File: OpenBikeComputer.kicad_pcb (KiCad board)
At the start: 4 copper layers, 80 x 80 mm, 56 parts, among them J1 USB_C_Receptacle_USB2.0_14P, J2 RJ45_Shielded, J3 RJ45_Shielded, J4 Micro_SD_Card_Det1, J5 Conn_01x24_Socket, J6 Conn_01x03_Pin, J7 Conn_01x05_Pin, U1 nRF52840-QIXX, U2 nPM1300-QEXX, U3 BQ298012RUGR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

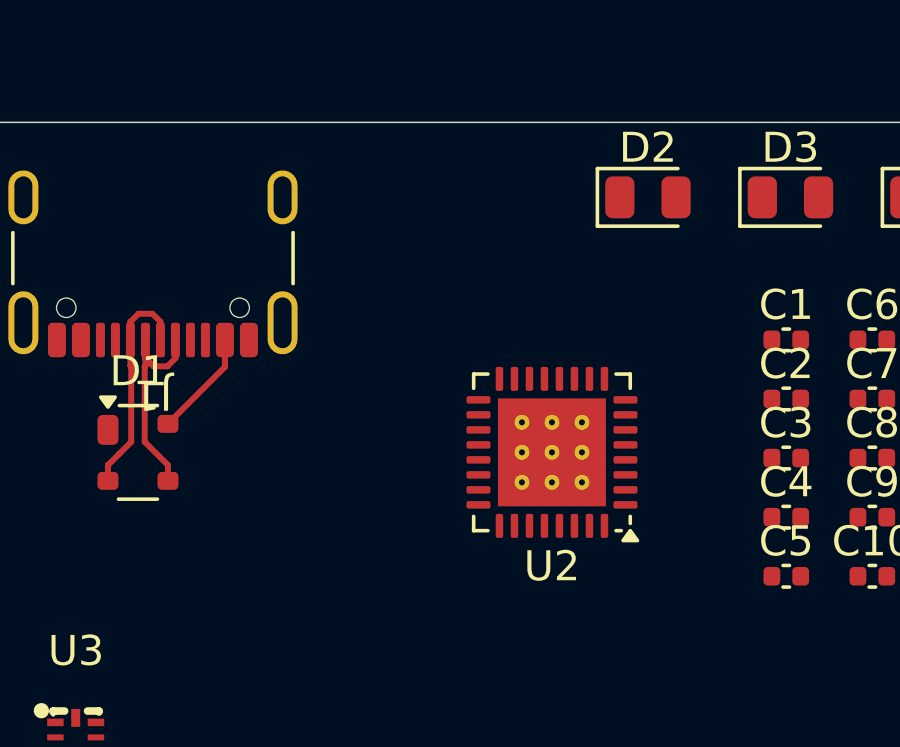
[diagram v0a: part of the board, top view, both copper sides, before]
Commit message: add inductor and crystal
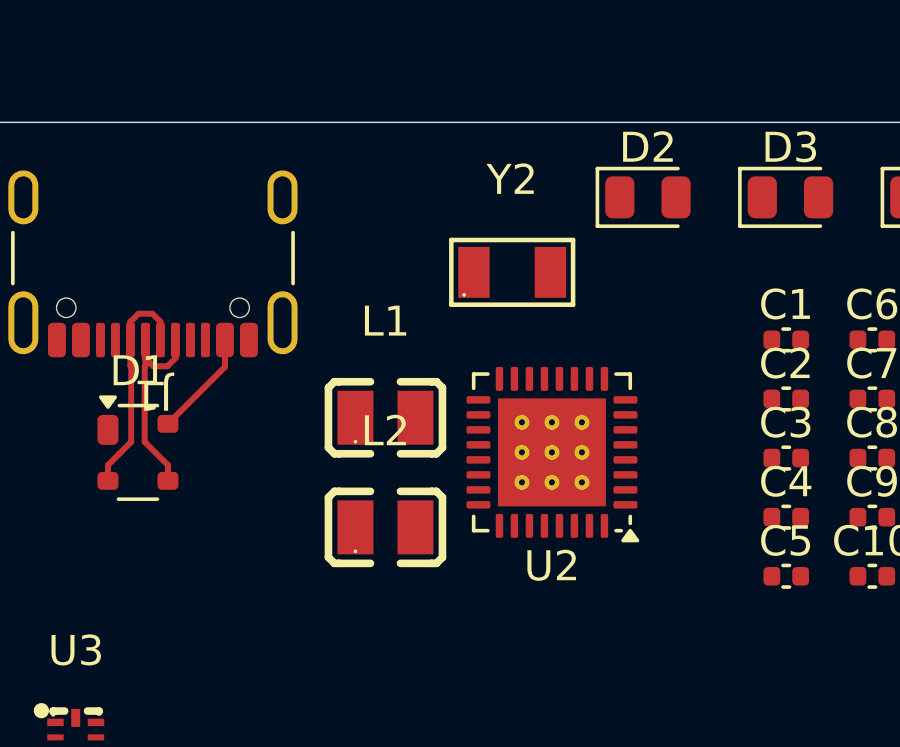
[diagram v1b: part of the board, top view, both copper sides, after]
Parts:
- added L1: 2.2uH, Library:L0806, F.Cu at (199.5, 84.8)
- added L2: 2.2uH, Library:L0806, F.Cu at (199.5, 88.5)
- added Y2: 32.768KHz, Library:CRYSTAL-SMD_L3.2-W1.5-1, F.Cu at (203.7, 80.0)

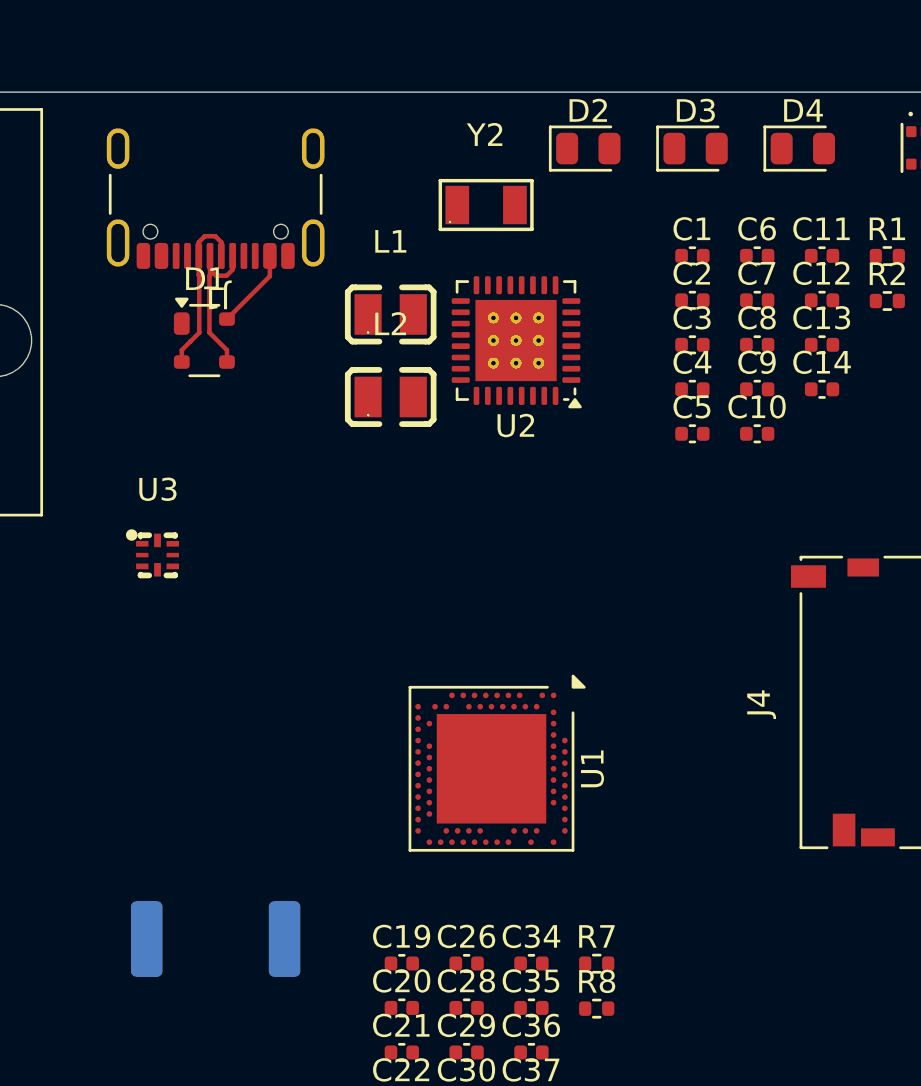
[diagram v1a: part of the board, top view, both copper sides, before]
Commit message: fixup design pcb clearances
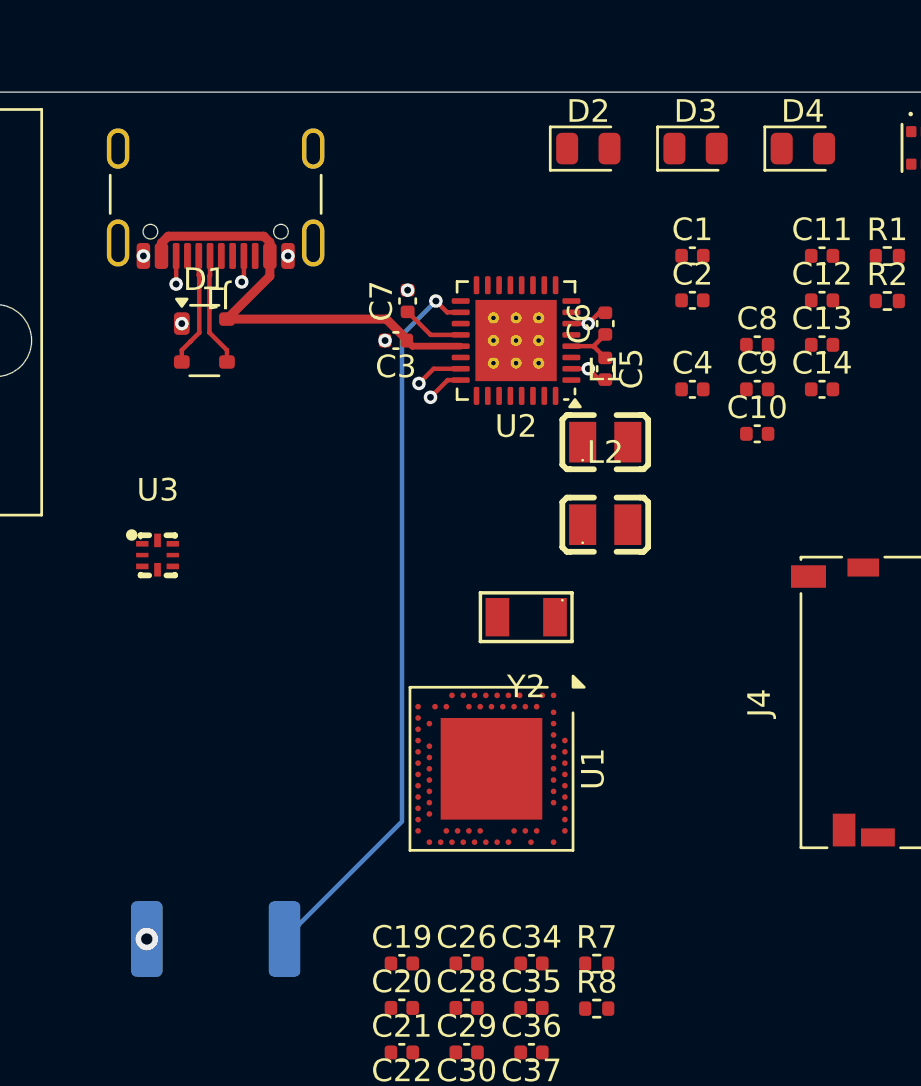
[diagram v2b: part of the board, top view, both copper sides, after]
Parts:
- moved Y2 18.3 mm to (205.5, 98.2), turned to 180 degrees
- moved C7 15.5 mm to (200.2, 84.2), turned to 90 degrees
- moved C3 13.1 mm to (199.7, 86.0), turned to 180 degrees
- moved L1 11.1 mm to (209.0, 90.5)
- moved L2 11.1 mm to (209.0, 94.2)
- moved C6 7.37 mm to (209.0, 85.2), turned to 90 degrees
- moved C5 4.82 mm to (209.0, 87.2), turned to -90 degrees
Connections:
- C5 pad 2: PVSS1 -> GND
- C6 pad 2: PVSS2 -> GND
- C8 pad 2: PVSS1 -> GND
- C9 pad 2: PVSS2 -> GND
- U2 pad 2: PVSS1 -> GND
- U2 pad 6: PVSS2 -> GND
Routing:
- net /Battery/NTC: track 0.00 -> 32.3 mm, vias 0 -> 1
- net VBUSIN: track 3.58 -> 20.7 mm
- net CC2: track 0.00 -> 16.4 mm, vias 0 -> 2
- net CC1: track 0.00 -> 13.1 mm, vias 0 -> 2
- net VSYS: track 0.00 -> 5.22 mm
- net GND: track 0.00 -> 3.40 mm, vias 0 -> 8
- net D-: track 7.46 -> 5.03 mm
- net D+: track 7.46 -> 5.03 mm

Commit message: use separate i2c bus for PMIC
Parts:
- added R10: 10k, Resistor_SMD:R_0402_1005Metric, F.Cu at (208.6, 120.0)
- added R9: 10k, Resistor_SMD:R_0402_1005Metric, F.Cu at (208.6, 118.0)
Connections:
- R7 pad 2: /MCU/SCL -> /MCU/SCL1
- R8 pad 2: /MCU/SDA -> /MCU/SDA1
- U1 pad AC15: unconnected-(U1-P0.19-PadAC15) -> /MCU/SDA2
- U1 pad AD20: unconnected-(U1-P0.24-PadAD20) -> /MCU/SCL2
- U1 pad L1: /MCU/SDA -> /MCU/SDA1
- U1 pad N1: /MCU/SCL -> /MCU/SCL1
- U2 pad 13: /MCU/SDA -> /MCU/SDA1
- U2 pad 14: /MCU/SCL -> /MCU/SCL1
- U2 pad 15: unconnected-(U2-SHPHLD-Pad15) -> Net-(U2-SHPHLD)
- U6 pad 13: /MCU/SCL -> /MCU/SCL2
- U6 pad 14: /MCU/SDA -> /MCU/SDA2
- U7 pad 3: /MCU/SDA -> /MCU/SDA2
- U7 pad 4: /MCU/SCL -> /MCU/SCL2
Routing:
- net D-: track 5.03 -> 7.46 mm
- net D+: track 5.03 -> 7.46 mm

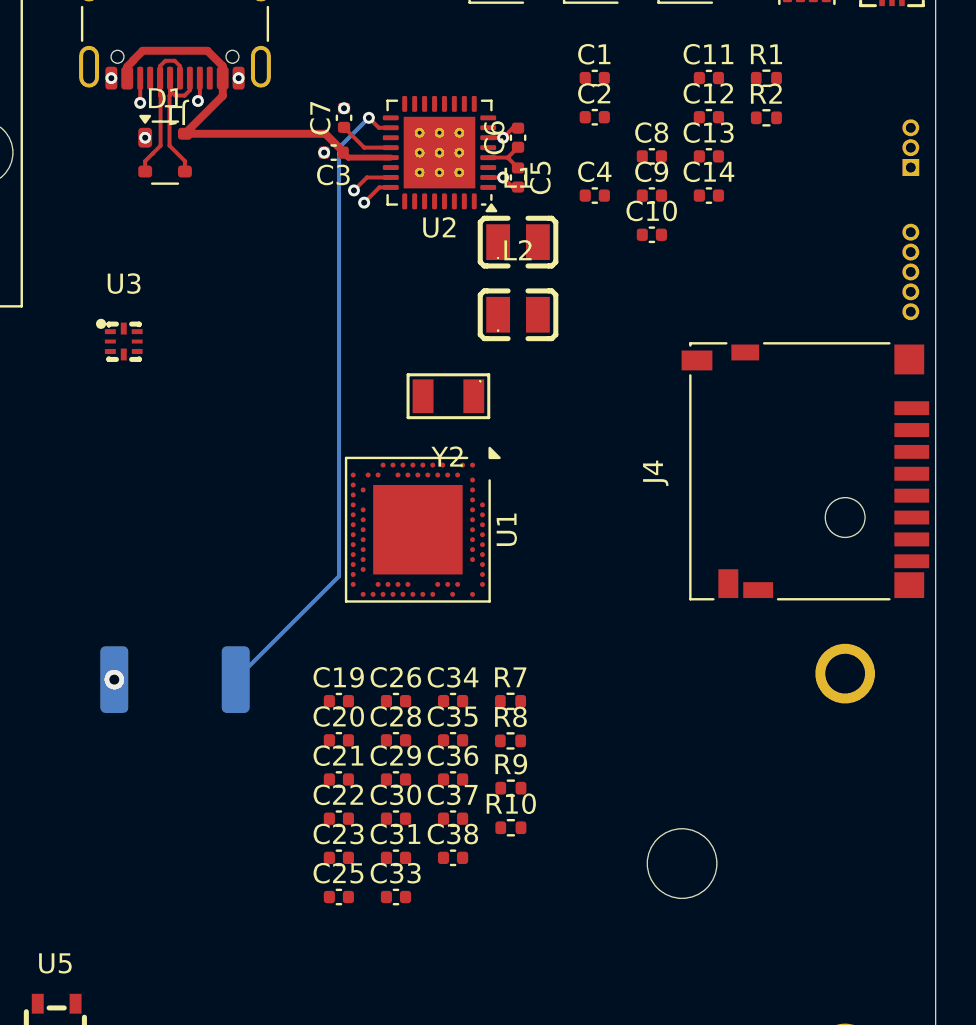
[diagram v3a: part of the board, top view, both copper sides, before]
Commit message: switch out SoC, stuff is in the air
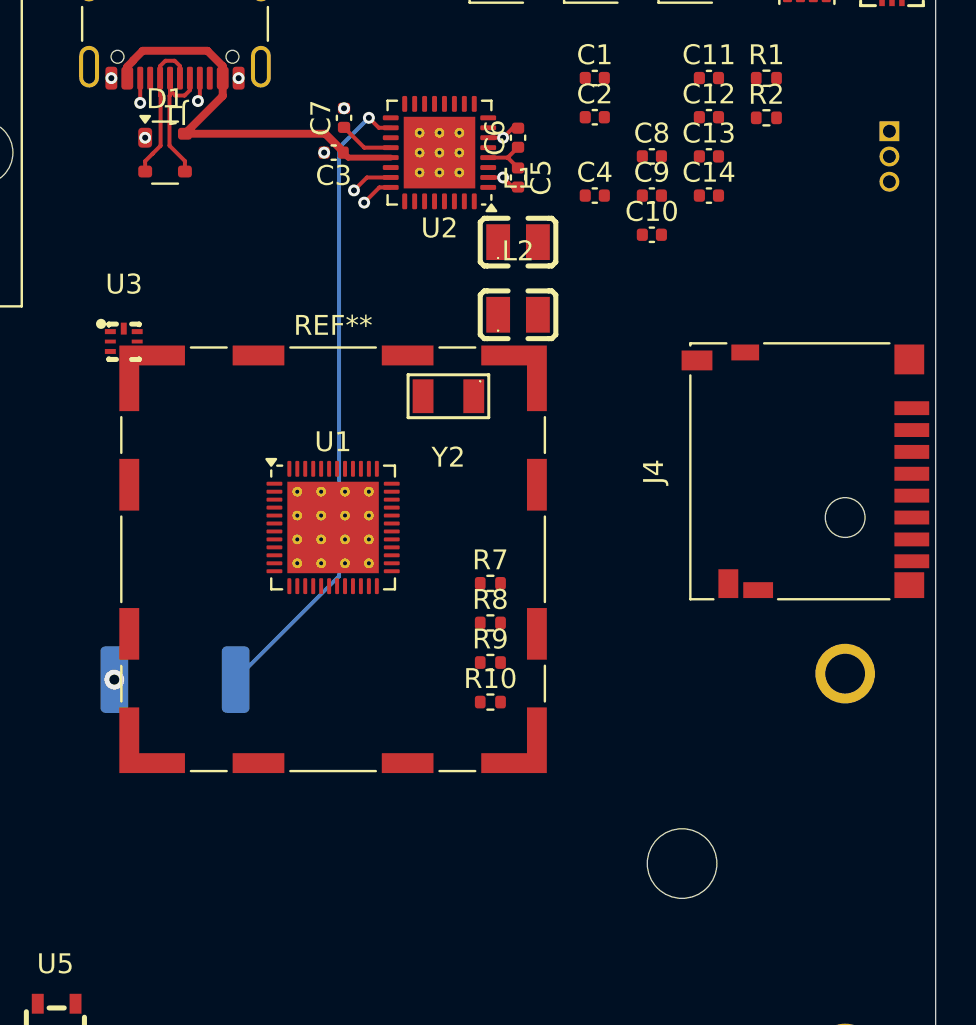
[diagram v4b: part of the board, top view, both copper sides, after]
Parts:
- removed C19, C20, C21, C22: 12pF, Capacitor_SMD:C_0402_1005Metric
- removed C23, C34: 4.7uF, Capacitor_SMD:C_0402_1005Metric
- removed C25, C35, C36, C38: 100nF, Capacitor_SMD:C_0402_1005Metric
- removed C26: 100pF, Capacitor_SMD:C_0402_1005Metric
- removed C28: 820pF, Capacitor_SMD:C_0402_1005Metric
- removed C29, C37: 1.0uF, Capacitor_SMD:C_0402_1005Metric
- removed C30: 47nF, Capacitor_SMD:C_0402_1005Metric
- removed C31, C33: 0.5pF, Capacitor_SMD:C_0402_1005Metric
- removed J7: Conn_01x05_Pin, Connector_PinHeader_1.00mm:PinHeader_1x05_P1.00mm_Vertical
- added REF**: Wuerth_36103205_20x20mm, RF_Shielding:Wuerth_36103205_20x20mm, F.Cu at (199.7, 106.5)
- J6: footprint Connector_PinHeader_1.00mm:PinHeader_1x03_P1.00mm_Vertical -> Connector_PinHeader_1.27mm:PinHeader_1x03_P1.27mm_Vertical
- U1: value nRF52840-QIXX -> nRF54L15-QFXX; footprint Package_DFN_QFN:Nordic_AQFN-73-1EP_7x7mm_P0.5mm -> Package_DFN_QFN:QFN-48-1EP_6x6mm_P0.4mm_EP4.6x4.6mm_ThermalVias
- moved R10 6.40 mm to (207.6, 113.6)
- moved R9 6.40 mm to (207.6, 111.6)
- moved R7 6.02 mm to (207.6, 107.7)
- moved R8 6.02 mm to (207.6, 109.7)
- moved U1 4.26 mm to (199.7, 104.8), turned to 0 degrees
- moved J6 1.09 mm to (227.7, 84.9)
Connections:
- C4 pad 1: /MCU/VBUS -> /Power/VUSBOUT
- D1 pad 2: D+ -> unconnected-(D1-I/O1-Pad2)
- D1 pad 3: D- -> unconnected-(D1-I/O2-Pad3)
- J1 pad A6: D+ -> unconnected-(J1-D+-PadA6)
- J1 pad A7: D- -> unconnected-(J1-D--PadA7)
- J1 pad B6: D+ -> unconnected-(J1-D+-PadB6)
- J1 pad B7: D- -> unconnected-(J1-D--PadB7)
- U2 pad 22: /MCU/VBUS -> /Power/VUSBOUT
- Y2 pad 1: Net-(U1-P0.00/XL1) -> Net-(U1-P1.00)
- Y2 pad 2: Net-(U1-P0.01/XL2) -> Net-(U1-P1.01)
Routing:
- net (no net): track 0.00 -> 14.9 mm
- net D+: track 7.46 -> 0.00 mm
- net D-: track 7.46 -> 0.00 mm

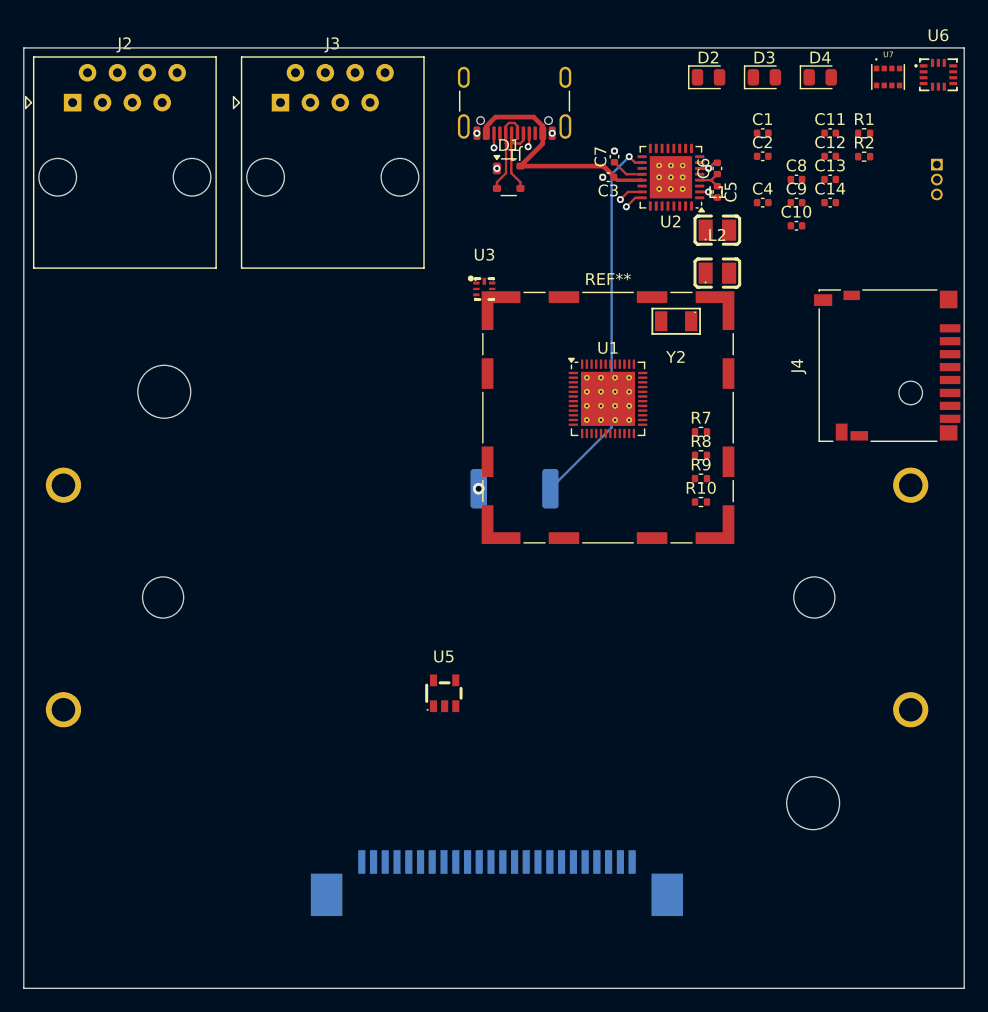
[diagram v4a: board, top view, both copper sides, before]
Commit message: re-integrate all components + add BT antenna
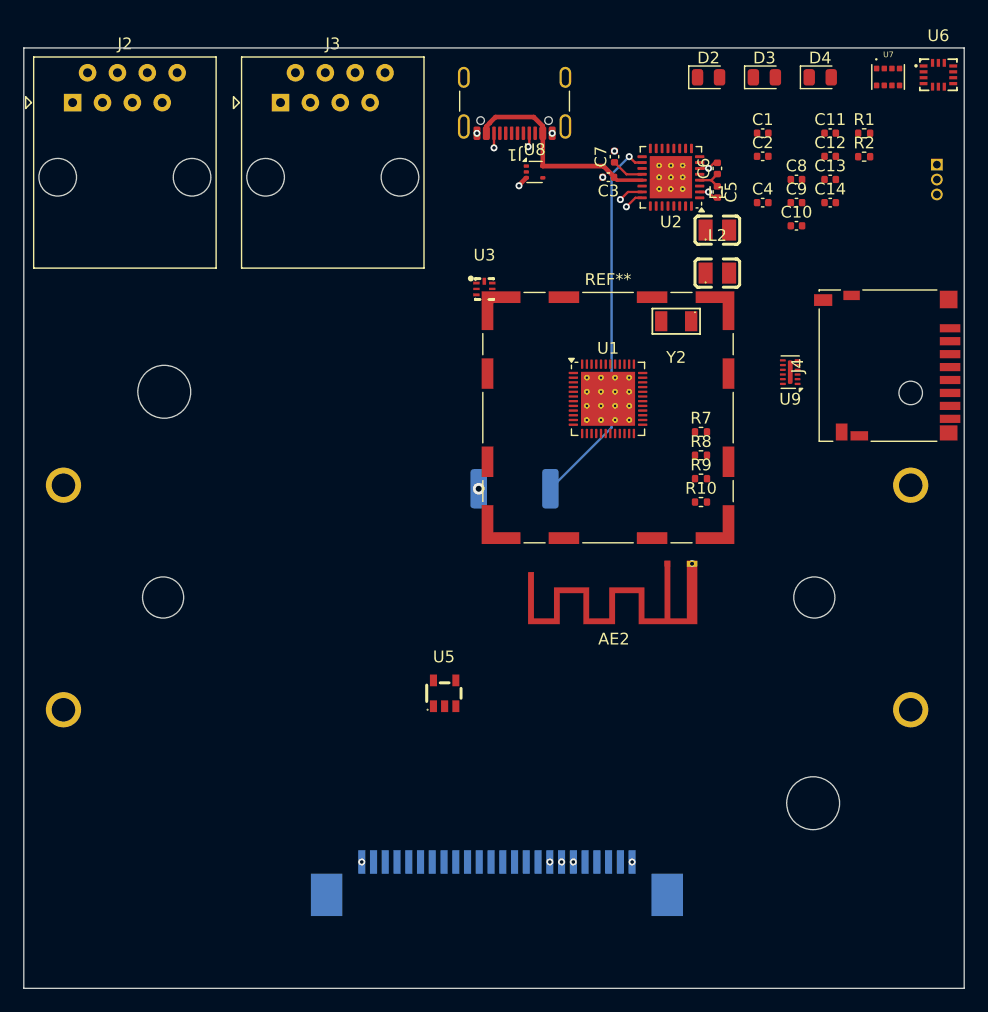
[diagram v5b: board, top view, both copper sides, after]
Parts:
- removed D1: PRTR5V0U2X, Package_TO_SOT_SMD:SOT-143
- added AE2: Antenna_Shield, RF_Antenna:Texas_SWRA117D_2.4GHz_Right, F.Cu at (204.8, 118.9)
- added U8: TPD3E001DRLR, Package_TO_SOT_SMD:SOT-553, F.Cu at (193.4, 85.5)
- added U9: TPD6F003, Package_SON:Texas_R-PWSON-N12_EP0.4x2mm, F.Cu at (215.2, 102.6)
- C1: value 1.0uF -> 0.1pF
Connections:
- J4 pad 1: unconnected-(J4-DAT2-Pad1) -> Net-(J4-DAT2)
- J4 pad 2: SD_CS -> Net-(J4-DAT3/CD)
- J4 pad 3: SD_MOSI -> Net-(J4-CMD)
- J4 pad 5: SD_SCLK -> Net-(J4-CLK)
- J4 pad 7: SD_MISO -> Net-(J4-DAT0)
- J4 pad 8: unconnected-(J4-DAT1-Pad8) -> Net-(J4-DAT1)
- J5 pad 3: VDDIO -> Net-(J5-Pin_3)
- J5 pad 4: Net-(J5-Pin_4) -> VDDIO
- J5 pad 5: unconnected-(J5-Pin_5-Pad5) -> VDDIO
- J5 pad 6: unconnected-(J5-Pin_6-Pad6) -> GND
- J5 pad 7: unconnected-(J5-Pin_7-Pad7) -> GND
- J5 pad 8: unconnected-(J5-Pin_8-Pad8) -> GND
- R10 pad 2: /MCU/SCL2 -> SCL2
- R7 pad 2: /MCU/SCL1 -> SCL1
- R8 pad 2: /MCU/SDA1 -> SDA1
- R9 pad 2: /MCU/SDA2 -> SDA2
- U1 pad 11: unconnected-(U1-P2.00-Pad11) -> DETECT1
- U1 pad 12: unconnected-(U1-P2.01-Pad12) -> DETECT2
- U1 pad 13: unconnected-(U1-P2.02-Pad13) -> BUT1
- U1 pad 14: unconnected-(U1-P2.03-Pad14) -> BUT2
- U1 pad 15: unconnected-(U1-P2.04-Pad15) -> BUT3
- U1 pad 16: unconnected-(U1-P2.05-Pad16) -> BUT4
- U1 pad 17: unconnected-(U1-P2.06-Pad17) -> /Display/SCLK
- U1 pad 18: unconnected-(U1-P2.07-Pad18) -> /MCU/MOTION_INT
- U1 pad 19: unconnected-(U1-P2.08-Pad19) -> /Display/MOSI
- U1 pad 23: unconnected-(U1-P0.00-Pad23) -> SD_DETECT
- U1 pad 24: unconnected-(U1-P0.01-Pad24) -> SD_CS
- U1 pad 27: unconnected-(U1-P0.02-Pad27) -> SD_MISO
- U1 pad 28: unconnected-(U1-P0.03-Pad28) -> SD_SCLK
- U1 pad 29: unconnected-(U1-P0.04-Pad29) -> SD_MOSI
- U1 pad 3: unconnected-(U1-P1.02-Pad3) -> Net-(U1-P1.02)
- U1 pad 37: unconnected-(U1-P1.09-Pad37) -> SDA2
- U1 pad 38: unconnected-(U1-P1.10-Pad38) -> SDA1
- U1 pad 39: unconnected-(U1-P1.11-Pad39) -> SCL1
- U1 pad 4: unconnected-(U1-P1.03-Pad4) -> Net-(U1-P1.03)
- U1 pad 41: unconnected-(U1-P1.13-Pad41) -> /MCU/RESET
- U1 pad 42: unconnected-(U1-P1.14-Pad42) -> /MCU/INT
- U1 pad 9: unconnected-(U1-P1.08-Pad9) -> SCL2
- U2 pad 13: /MCU/SDA1 -> SDA1
- U2 pad 14: /MCU/SCL1 -> SCL1
- U6 pad 13: /MCU/SCL2 -> SCL2
- U6 pad 14: /MCU/SDA2 -> SDA2
- U7 pad 3: /MCU/SDA2 -> SDA2
- U7 pad 4: /MCU/SCL2 -> SCL2
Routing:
- net (no net): track 14.9 -> 0.00 mm
- net VBUSIN: track 21.1 -> 18.4 mm
- net GND: track 3.40 -> 4.33 mm, vias 8 -> 14
